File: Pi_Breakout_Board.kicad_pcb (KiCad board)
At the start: 2 copper layers, 56.5 x 65 mm, 74 parts, among them J1 Raspberry_Pi_2_3, J2 Conn_02x04_Odd_Even heater he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, J3 Conn_02x08_Odd_Even thermisto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, J4 Screw_Terminal_01x02, J5 Conn_01x08_Male, J6 Conn_01x08_Male, J7 Conn_01x02_Female, J8 Conn_01x03_Male, Q1 Q_NMOS_GDSD, Q2 Q_NMOS_GDSD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

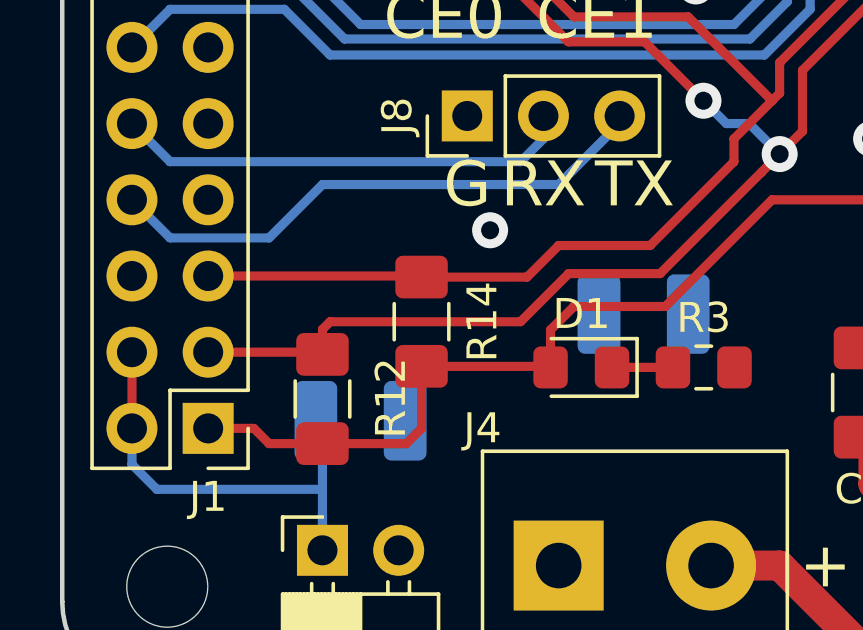
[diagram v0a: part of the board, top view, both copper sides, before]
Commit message: add TVS diode
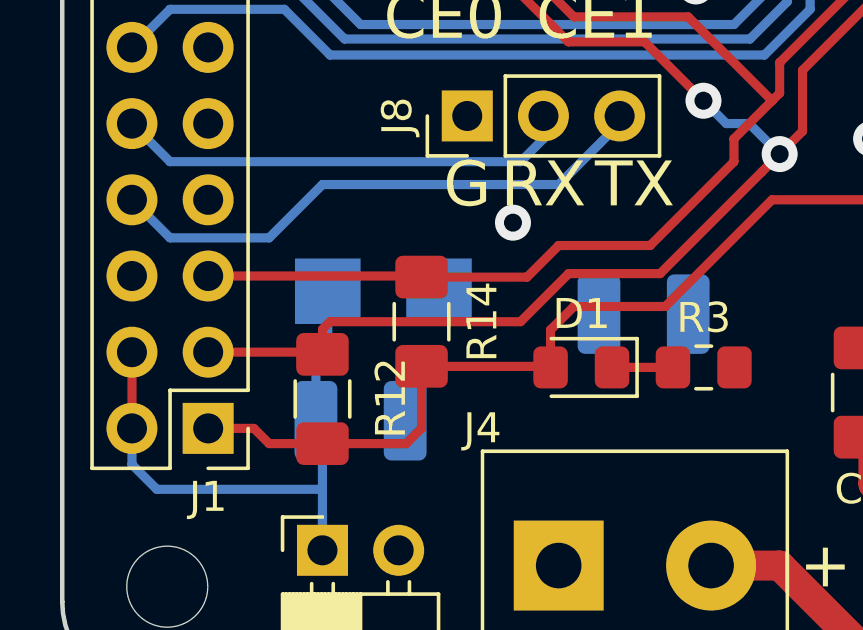
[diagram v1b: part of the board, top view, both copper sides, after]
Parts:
- added D5: SMBJ5.0A, footprints:SMBJ5.0A, B.Cu at (60.7, 136.7)
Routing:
- net +5V: track 16.1 -> 20.6 mm
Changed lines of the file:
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@@
     (thickness 1.6)
     (drawings 38)
-    (tracks 485)
+    (tracks 488)
     (zones 0)
-    (modules 74)
+    (modules 75)
     (nets 75)
   )
@@
     )
   )
+  (module footprints:SMBJ5.0A (layer B.Cu)
+    (at 60.706 136.652)
+    (fp_text reference D5 (at 0 5.08) (layer B.SilkS)
+      (effects (font (size 1 1) (thickness 0.15)) (justify mirror))
+    )
+    (fp_text value SMBJ5.0A (at 0 3.81) (layer B.SilkS)
+      (effects (font (size 1 1) (thickness 0.15)) (justify mirror))
+    )
+    (fp_line (start -3.048 -1.3462) (end -3.2004 -1.3462) (layer B.CrtYd) (width 0.1524))
+    (fp_line (start -3.048 -2.2225) (end -3.048 -1.3462) (layer B.CrtYd) (width 0.1524))
+    (fp_line (start 3.048 -2.2225) (end -3.048 -2.2225) (layer B.CrtYd) (width 0.1524))
+    (fp_line (start 3.048 -1.3462) (end 3.048 -2.2225) (layer B.CrtYd) (width 0.1524))
+    (fp_line (start 3.2004 -1.3462) (end 3.048 -1.3462) (layer B.CrtYd) (width 0.1524))
+    (fp_line (start 3.2004 1.3462) (end 3.2004 -1.3462) (layer B.CrtYd) (width 0.1524))
+    (fp_line (start 3.048 1.3462) (end 3.2004 1.3462) (layer B.CrtYd) (width 0.1524))
+    (fp_line (start 3.048 2.2225) (end 3.048 1.3462) (layer B.CrtYd) (width 0.1524))
+    (fp_line (start -3.048 2.2225) (end 3.048 2.2225) (layer B.CrtYd) (width 0.1524))
+    (fp_line (start -3.048 1.3462) (end -3.048 2.2225) (layer B.CrtYd) (width 0.1524))
+    (fp_line (start -3.2004 1.3462) (end -3.048 1.3462) (layer B.CrtYd) (width 0.1524))
+    (fp_line (start -3.2004 -1.3462) (end -3.2004 1.3462) (layer B.CrtYd) (width 0.1524))
+    (fp_line (start 2.921 1.42494) (end 2.921 2.0955) (layer B.SilkS) (width 0.1524))
+    (fp_line (start -2.921 -1.42494) (end -2.921 -2.0955) (layer B.SilkS) (width 0.1524))
+    (fp_line (start -2.794 1.9685) (end -2.794 -1.9685) (layer B.Fab) (width 0.1524))
+    (fp_line (start 2.794 1.9685) (end -2.794 1.9685) (layer B.Fab) (width 0.1524))
+    (fp_line (start 2.794 -1.9685) (end 2.794 1.9685) (layer B.Fab) (width 0.1524))
+    (fp_line (start -2.794 -1.9685) (end 2.794 -1.9685) (layer B.Fab) (width 0.1524))
+    (fp_line (start -2.921 2.0955) (end -2.921 1.42494) (layer B.SilkS) (width 0.1524))
+    (fp_line (start 2.921 2.0955) (end -2.921 2.0955) (layer B.SilkS) (width 0.1524))
+    (fp_line (start 2.921 -2.0955) (end 2.921 -1.42494) (layer B.SilkS) (width 0.1524))
+    (fp_line (start -2.921 -2.0955) (end 2.921 -2.0955) (layer B.SilkS) (width 0.1524))
+    (fp_line (start -3.556 0.635) (end -3.556 -0.635) (layer B.SilkS) (width 0.1524))
+    (fp_line (start -4.318 0) (end -3.556 -0.127) (layer B.SilkS) (width 0.1524))
+    (fp_line (start -4.318 0) (end -3.556 -0.254) (layer B.SilkS) (width 0.1524))
+    (fp_line (start -4.318 0) (end -3.556 -0.381) (layer B.SilkS) (width 0.1524))
+    (fp_line (start -4.318 0) (end -3.556 -0.508) (layer B.SilkS) (width 0.1524))
+    (fp_line (start -4.318 0) (end -3.556 -0.635) (layer B.SilkS) (width 0.1524))
+    (fp_line (start -4.318 0) (end -3.556 0.127) (layer B.SilkS) (width 0.1524))
+    (fp_line (start -4.318 0) (end -3.556 0.254) (layer B.SilkS) (width 0.1524))
+    (fp_line (start -4.318 0) (end -3.556 0.381) (layer B.SilkS) (width 0.1524))
+    (fp_line (start -4.318 0) (end -3.556 0.508) (layer B.SilkS) (width 0.1524))
+    (fp_line (start -4.318 0) (end -3.556 0.635) (layer B.SilkS) (width 0.1524))
+    (fp_line (start -4.318 0.635) (end -4.318 -0.635) (layer B.SilkS) (width 0.1524))
+    (fp_line (start -3.302 0) (end -4.572 0) (layer B.SilkS) (width 0.1524))
+    (fp_line (start -3.556 0.635) (end -3.556 -0.635) (layer B.Fab) (width 0.1524))
+    (fp_line (start -4.318 0) (end -3.556 -0.127) (layer B.Fab) (width 0.1524))
+    (fp_line (start -4.318 0) (end -3.556 -0.254) (layer B.Fab) (width 0.1524))
+    (fp_line (start -4.318 0) (end -3.556 -0.381) (layer B.Fab) (width 0.1524))
+    (fp_line (start -4.318 0) (end -3.556 -0.508) (layer B.Fab) (width 0.1524))
+    (fp_line (start -4.318 0) (end -3.556 -0.635) (layer B.Fab) (width 0.1524))
+    (fp_line (start -4.318 0) (end -3.556 0.127) (layer B.Fab) (width 0.1524))
+    (fp_line (start -4.318 0) (end -3.556 0.254) (layer B.Fab) (width 0.1524))
+    (fp_line (start -4.318 0) (end -3.556 0.381) (layer B.Fab) (width 0.1524))
+    (fp_line (start -4.318 0) (end -3.556 0.508) (layer B.Fab) (width 0.1524))
+    (fp_line (start -4.318 0) (end -3.556 0.635) (layer B.Fab) (width 0.1524))
+    (fp_line (start -4.318 0.635) (end -4.318 -0.635) (layer B.Fab) (width 0.1524))
+    (fp_line (start -3.302 0) (end -4.572 0) (layer B.Fab) (width 0.1524))
+    (fp_text user * (at -3.81 5.08) (layer B.Fab)
+      (effects (font (size 1 1) (thickness 0.15)) (justify mirror))
+    )
+    (fp_text user * (at -2.54 5.08) (layer B.SilkS)
+      (effects (font (size 1 1) (thickness 0.15)) (justify mirror))
+    )
+    (fp_text user "Copyright 2016 Accelerated Designs. All rights reserved." (at 0 0) (layer Cmts.User)
+      (effects (font (size 0.127 0.127) (thickness 0.002)))
+    )
+    (pad 2 smd rect (at 1.8542 0 270) (size 2.1844 2.1844) (layers B.Cu B.Paste B.Mask)
+      (net 5 GND))
+    (pad 1 smd rect (at -1.8542 0 270) (size 2.1844 2.1844) (layers B.Cu B.Paste B.Mask)
+      (net 12 +5V))
+  )
   (gr_text 3 (at 98.298 137.16) (layer F.SilkS)
     (effects (font (size 1.5 1.5) (thickness 0.3)))
@@
   (via (at 60.452 97.536) (size 1.2) (drill 0.6) (layers F.Cu B.Cu) (net 5))
   (via (at 76.962 131.572) (size 1.2) (drill 0.6) (layers F.Cu B.Cu) (net 5))
-  (via (at 64.262 134.62) (size 1.2) (drill 0.6) (layers F.Cu B.Cu) (net 5))
+  (via (at 65.024 134.366) (size 1.2) (drill 0.6) (layers F.Cu B.Cu) (net 5))
   (via (at 99.06 140.462) (size 1.2) (drill 0.6) (layers F.Cu B.Cu) (net 5))
   (via (at 62.738 88.9) (size 1.2) (drill 0.6) (layers F.Cu B.Cu) (net 5))
@@
   (segment (start 58.674 145.288) (end 58.674 143.256) (width 0.3048) (layer B.Cu) (net 12) (status 10))
   (segment (start 58.674 143.256) (end 58.674 143.002) (width 0.3048) (layer B.Cu) (net 12))
+  (segment (start 58.8518 136.652) (end 58.8518 138.2522) (width 0.3048) (layer B.Cu) (net 12))
+  (segment (start 58.4565 138.6475) (end 58.4565 140.97) (width 0.3048) (layer B.Cu) (net 12))
+  (segment (start 58.8518 138.2522) (end 58.4565 138.6475) (width 0.3048) (layer B.Cu) (net 12))
   (segment (start 80.518 141.891677) (end 80.61622 141.793457) (width 1) (layer B.Cu) (net 26) (status 30))
   (segment (start 80.518 146) (end 80.518 141.891677) (width 1) (layer B.Cu) (net 26) (status 30))
@@
     (connect_pads (clearance 0.508))
     (min_thickness 0.254)
-    (fill (arc_segments 16) (thermal_gap 0.508) (thermal_bridge_width 0.508))
+    (fill yes (arc_segments 16) (thermal_gap 0.508) (thermal_bridge_width 0.508))
     (polygon
       (pts
@@
     (connect_pads (clearance 0.508))
     (min_thickness 0.254)
-    (fill (arc_segments 16) (thermal_gap 0.508) (thermal_bridge_width 0.508))
+    (fill yes (arc_segments 16) (thermal_gap 0.508) (thermal_bridge_width 0.508))
     (polygon
       (pts

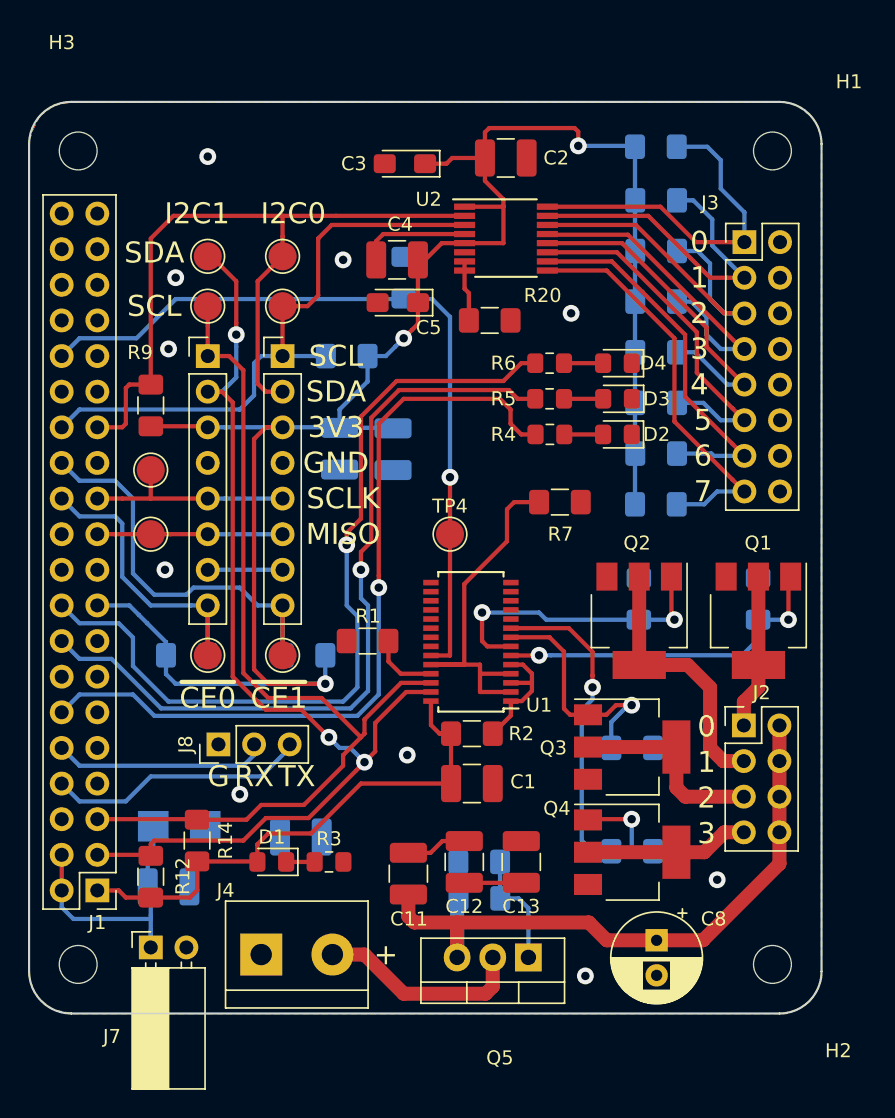
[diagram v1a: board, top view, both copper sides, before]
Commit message: misc placement changes
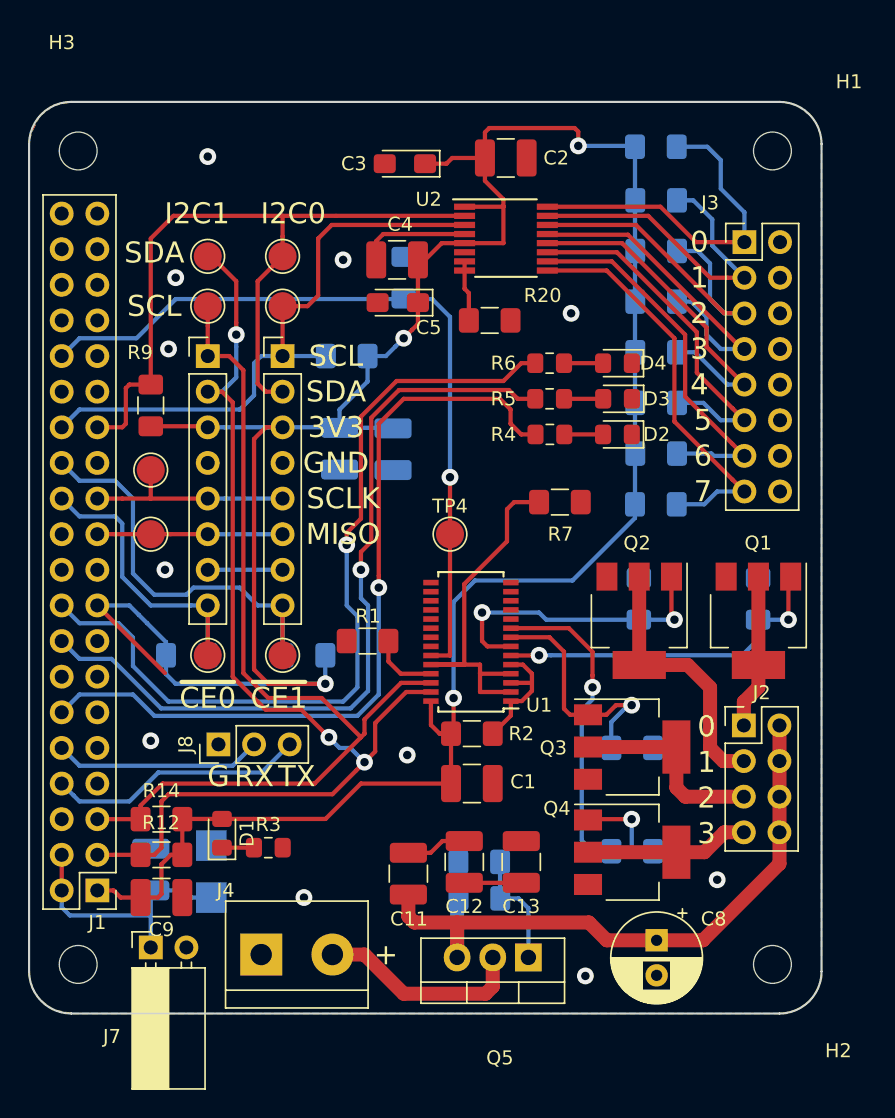
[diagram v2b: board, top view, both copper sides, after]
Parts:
- C9: moved to F.Cu
- moved C9 10.8 mm to (59.4, 141.7)
- moved R3 4.44 mm to (67.1, 138.2)
- moved D1 4.09 mm to (63.8, 137.2), turned to 90 degrees
- moved D5 3.95 mm to (63.0, 139.9), turned to 90 degrees
- moved R14 2.96 mm to (59.4, 136.1), turned to 180 degrees
- moved C10 1.77 mm to (58.7, 139.7), turned to 90 degrees
- moved R12 1.74 mm to (59.4, 138.7), turned to 180 degrees
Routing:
- net +3V3: track 176.6 -> 210.1 mm, vias 3 -> 4
- net +5V: track 20.6 -> 18.9 mm
- net SDA1: track 76.0 -> 77.4 mm
- net GND: vias 10 -> 12

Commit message: more routing updates + new gerbers generated. Ready to try and spin this
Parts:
- moved D1 1.61 mm to (64.3, 138.7), turned to 180 degrees
- moved R3 1.37 mm to (68.3, 138.7)
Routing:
- net +3V3: track 210.1 -> 204.6 mm
- net SDA1: track 77.4 -> 75.6 mm
- net SCL1: track 67.4 -> 66.6 mm
- net GND: vias 12 -> 11
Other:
- board text added: "CS"
- board text added: "MOSI"
